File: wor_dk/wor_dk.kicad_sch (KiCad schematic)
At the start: 5 parts

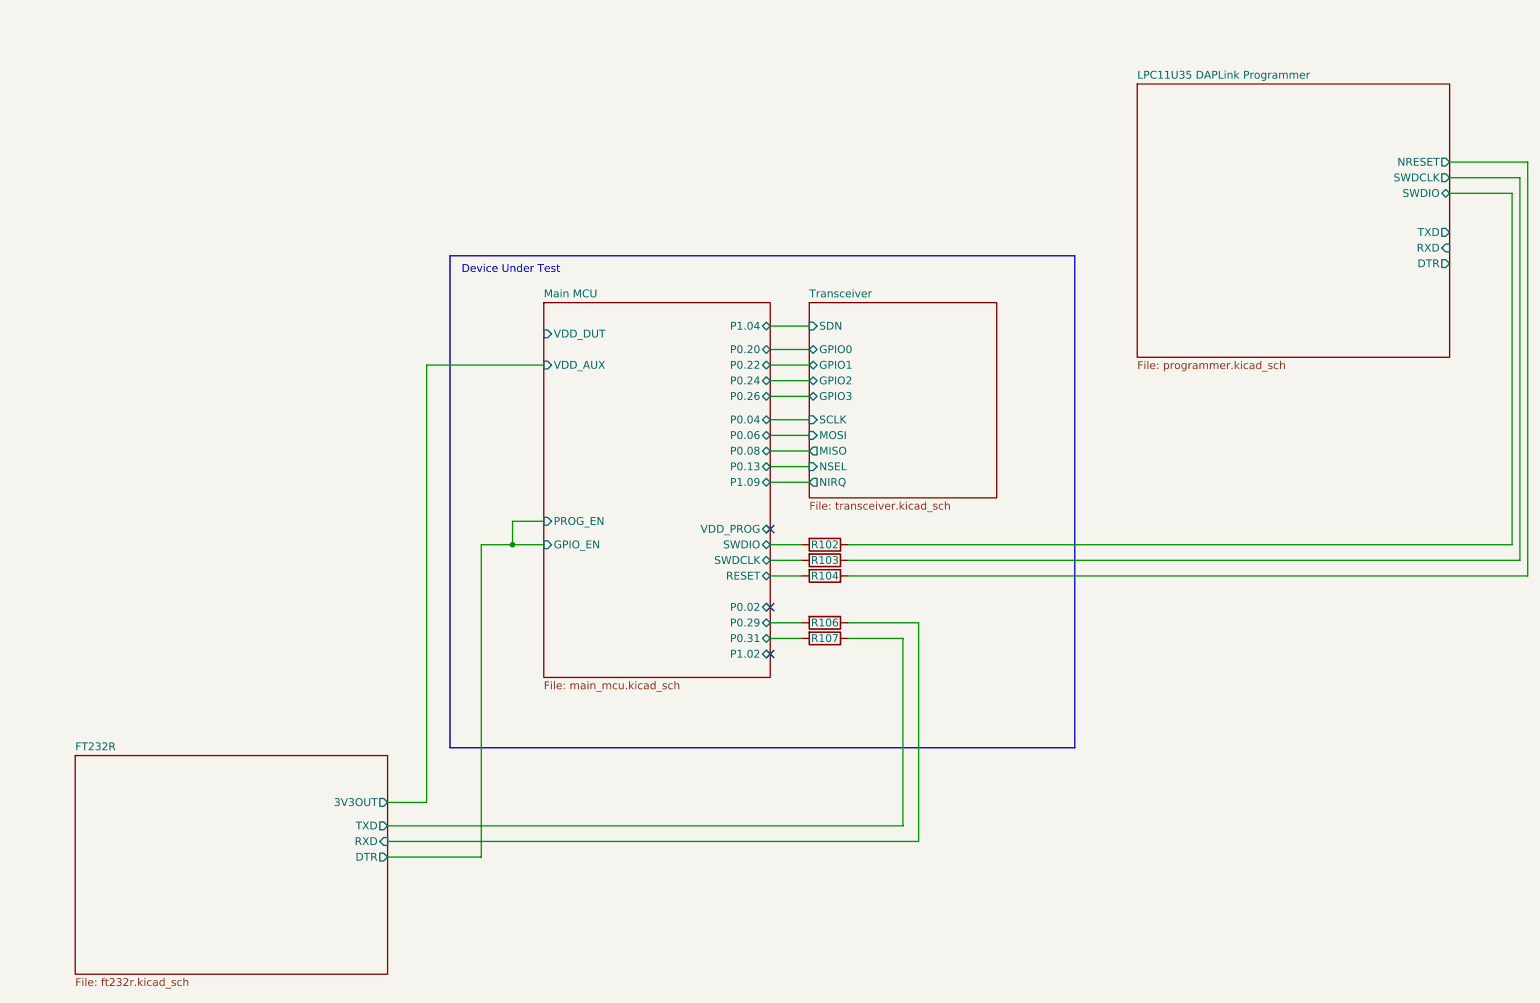
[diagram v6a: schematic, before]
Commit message: wor_dk: top-level connections & cleanup
- top-level connections for TMUX control & UART done (selection
  between FTDI and DAP Link via jumpers)
- all ERC errors & warnings cleaned up
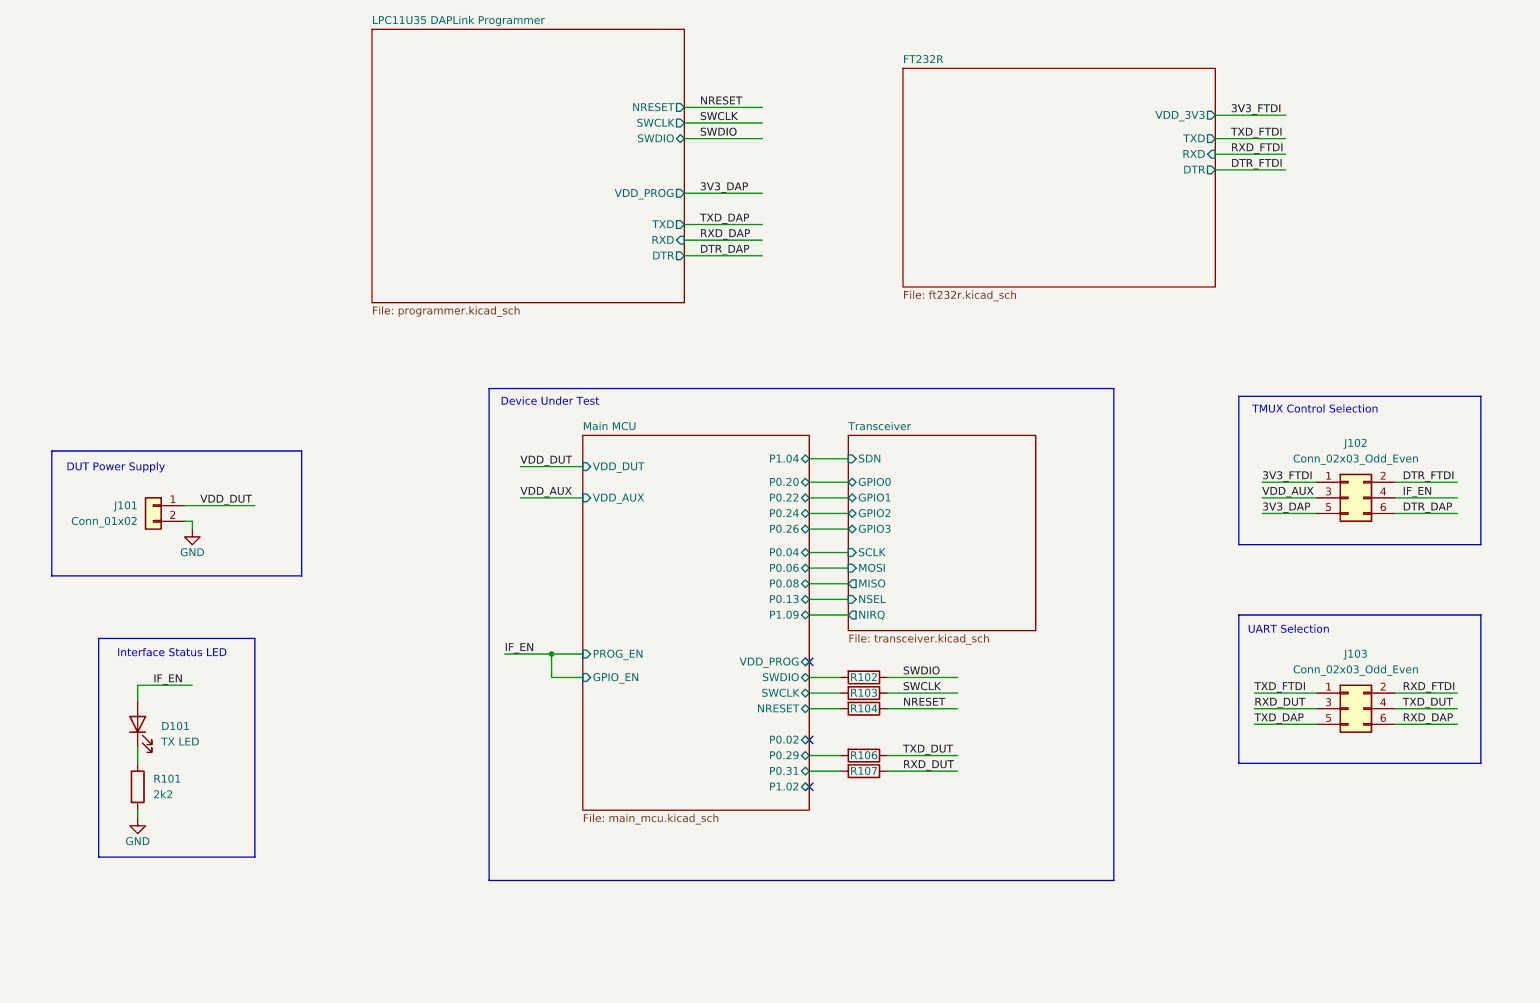
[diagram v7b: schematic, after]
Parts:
- added D101: TX LED, LED_SMD:LED_0805_2012Metric, symbol Device:LED
- added J101: Conn_01x02, symbol Connector_Generic:Conn_01x02
- added J102, J103: Conn_02x03_Odd_Even, symbol Connector_Generic:Conn_02x03_Odd_Even
- added R101: 2k2, Resistor_SMD:R_0402_1005Metric, symbol Device:R
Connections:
- net FT232R/RXD renamed TXD_DUT
- net TXD_DUT: now also J103.4 (Pin_4)
- net FT232R/TXD renamed RXD_DUT
- net RXD_DUT: now also J103.3 (Pin_3)
- net LPC11U35 DAPLink Programmer/NRESET renamed NRESET
- net LPC11U35 DAPLink Programmer/SWDCLK renamed SWCLK
- net LPC11U35 DAPLink Programmer/SWDIO renamed SWDIO
- net Main MCU/RESET renamed Main MCU/NRESET
- net Main MCU/SWDCLK renamed Main MCU/SWCLK
- new net: D101.1 (K), R101.1
- new net 3V3_DAP: J102.5 (Pin_5)
- new net 3V3_FTDI: J102.1 (Pin_1)
- new net DTR_DAP: J102.6 (Pin_6)
- new net DTR_FTDI: J102.2 (Pin_2)
- new net GND: J101.2 (Pin_2), R101.2
- new net IF_EN: D101.2 (A), J102.4 (Pin_4)
- new net RXD_DAP: J103.6 (Pin_6)
- new net RXD_FTDI: J103.2 (Pin_2)
- new net TXD_DAP: J103.5 (Pin_5)
- new net TXD_FTDI: J103.1 (Pin_1)
- new net VDD_AUX: J102.3 (Pin_3)
- new net VDD_DUT: J101.1 (Pin_1)
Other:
- sheet FT232R ports: added VDD_3V3; removed 3V3OUT
- sheet LPC11U35 DAPLink Programmer ports: added SWCLK, VDD_PROG; removed SWDCLK
- sheet Main MCU ports: added NRESET, SWCLK; removed RESET, SWDCLK
- note added: "DUT Power Supply"
- note added: "Interface Status LED"
- note added: "TMUX Control Selection"
- note added: "UART Selection"
- moved on the sheet: R102, R103, R104, R106, R107

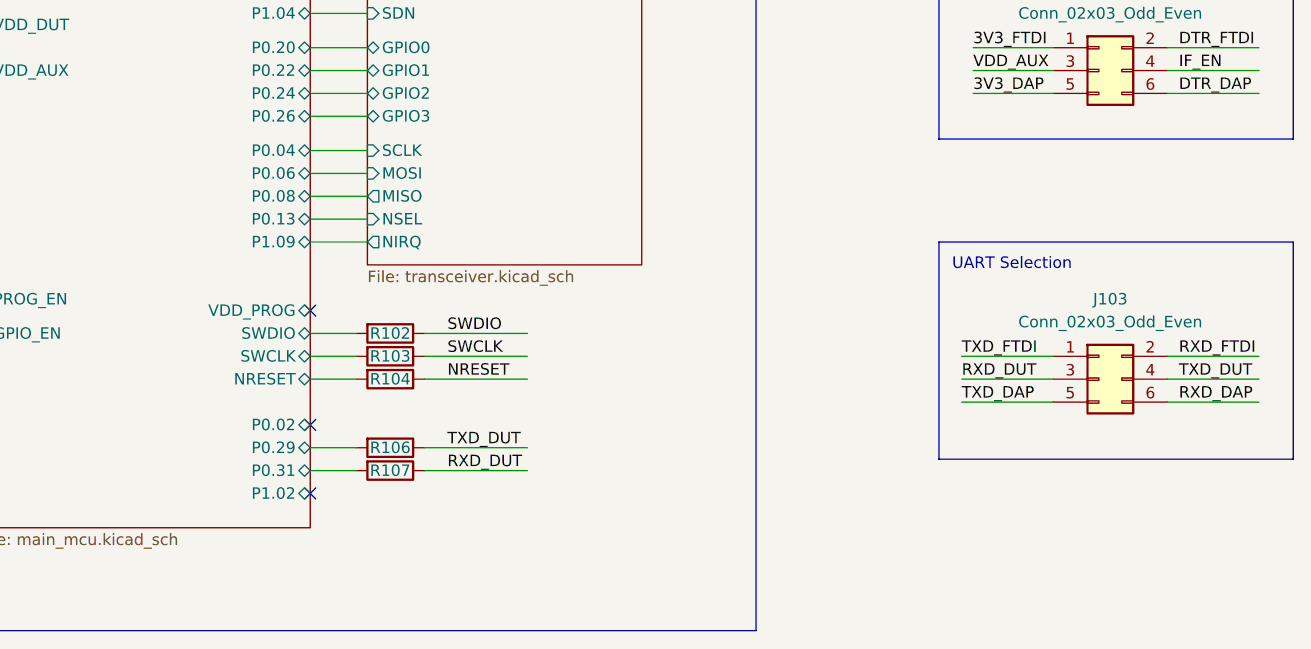
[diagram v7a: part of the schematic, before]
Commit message: wor_dk: cleanup & add test points & add pin headers
- test points are added for signals that only need to be measured to
  ensure proper functionality of the WoR DK
- pin headers are added for signals that may be useful during use of
  the WoR DK
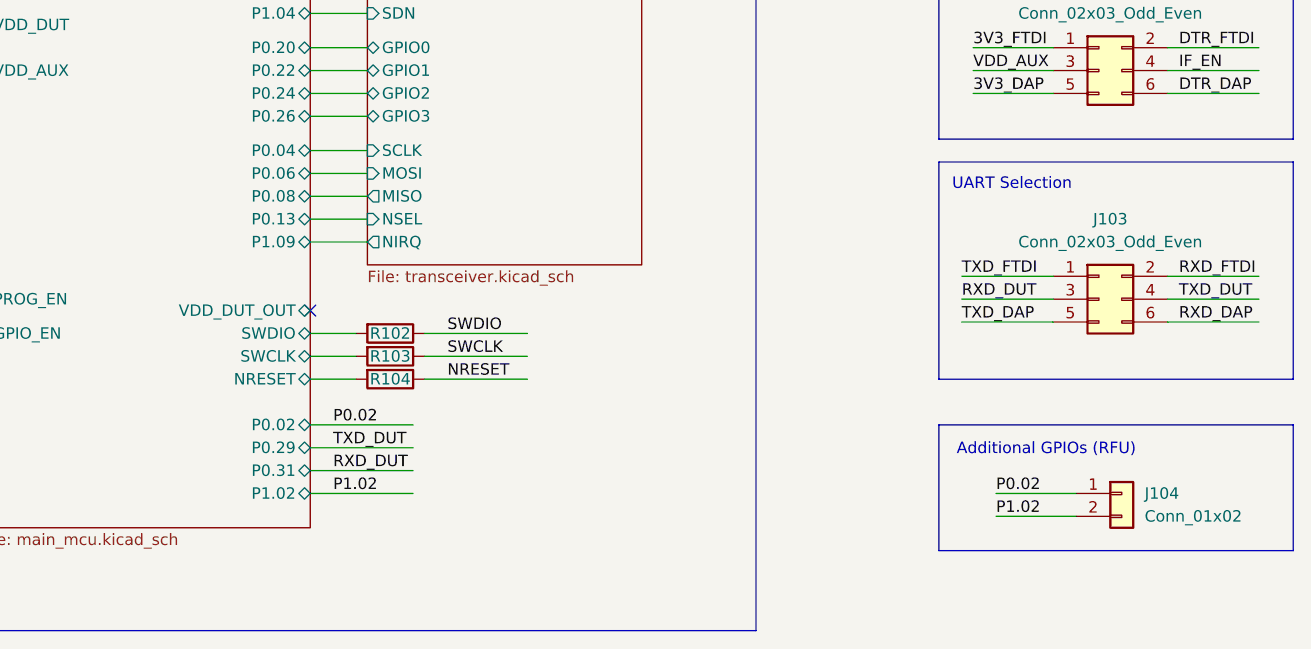
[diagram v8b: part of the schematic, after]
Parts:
- removed R106, R107: 0, symbol Device:R
- added J104: Conn_01x02, symbol Connector_Generic:Conn_01x02
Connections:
- new net P0.02: J104.1 (Pin_1)
- new net P1.02: J104.2 (Pin_2)
- no-connect marks 3 -> 1
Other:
- sheet Main MCU ports: added VDD_DUT_OUT; removed VDD_PROG
- note added: "Additional GPIOs (RFU)"
- moved on the sheet: J103
